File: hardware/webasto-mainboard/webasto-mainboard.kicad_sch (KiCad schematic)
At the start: 11 parts

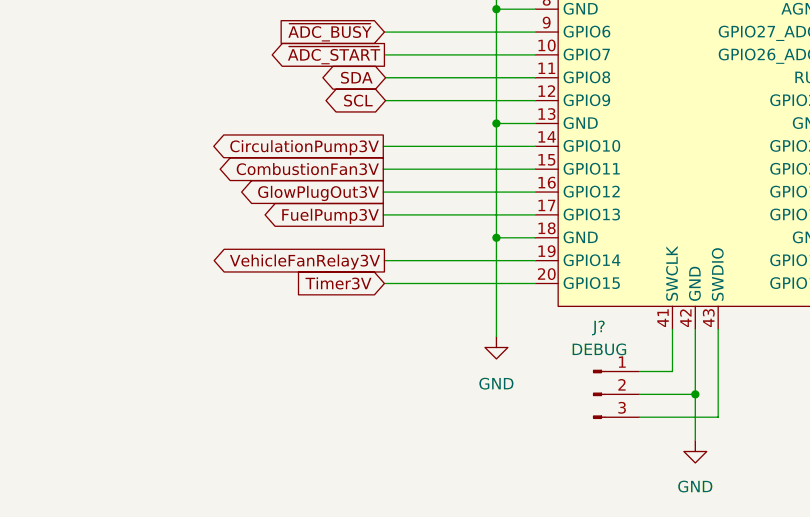
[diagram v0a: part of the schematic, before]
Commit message: Update schematics.  Had a better idea.
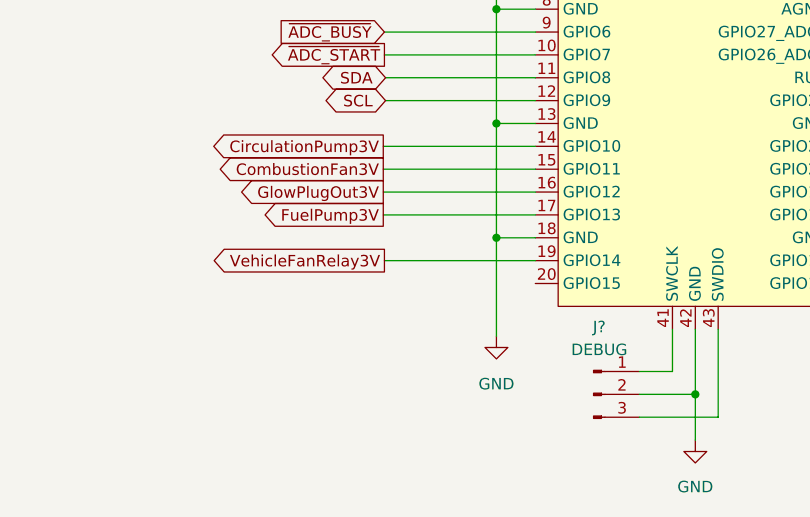
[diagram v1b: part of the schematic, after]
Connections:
- net Timer3V: no longer names the net of U?.20 (GPIO15)
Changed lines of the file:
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@@
-    (stroke (width 0) (type default) (color 0 0 0 0))
-  )
-  (wire (pts (xy 109.855 144.653) (xy 126.619 144.653))
     (stroke (width 0) (type default) (color 0 0 0 0))
   )
@@
     (effects (font (size 1.27 1.27)) (justify right))
     (property "Intersheet References" "${INTERSHEET_REFS}" (id 0) (at 97.4633 98.8536 0)
-      (effects (font (size 1.27 1.27)) (justify right) hide)
-    )
-  )
-  (global_label "Timer3V" (shape input) (at 109.855 144.653 180) (fields_autoplaced)
-    (effects (font (size 1.27 1.27)) (justify right))
-    (property "Intersheet References" "${INTERSHEET_REFS}" (id 0) (at 100.0033 144.5736 0)
       (effects (font (size 1.27 1.27)) (justify right) hide)
     )
@@
       (reference "#PWR?") (unit 1) (value "+3V3") (footprint "")
     )
-    (path "/4eba7f3e-81ac-47cd-894e-cb117f012064/47587680-3503-46f7-a060-696a9c2f2074"
-      (reference "#PWR?") (unit 1) (value "+12V") (footprint "")
-    )
     (path "/5110a3f4-f5cf-4cd3-83b3-796c134e4e4f"
       (reference "#PWR?") (unit 1) (value "GND") (footprint "")
@@
       (reference "#PWR?") (unit 1) (value "+12V") (footprint "")
     )
-    (path "/4eba7f3e-81ac-47cd-894e-cb117f012064/d24087ff-492d-4dd2-be32-3f2b4a040185"
-      (reference "#PWR?") (unit 1) (value "+3V3") (footprint "")
-    )
     (path "/a592a926-6607-470c-8c00-8883e576bafe/d398396e-9d5c-4d0b-9432-67c25da39db5"
       (reference "#PWR?") (unit 1) (value "GND") (footprint "")
@@
       (reference "Q?") (unit 1) (value "2N7002") (footprint "Package_TO_SOT_SMD:SOT-23")
     )
-    (path "/4eba7f3e-81ac-47cd-894e-cb117f012064/11a8a387-60ef-4daa-b1f2-6a2e648a2221"
-      (reference "Q?") (unit 1) (value "2N7002") (footprint "Package_TO_SOT_SMD:SOT-23")
-    )
     (path "/4eba7f3e-81ac-47cd-894e-cb117f012064/5e743317-dee2-44eb-9fd1-c8d94f723e4f"
       (reference "Q?") (unit 1) (value "2N7002") (footprint "Package_TO_SOT_SMD:SOT-23")
@@
       (reference "R?") (unit 1) (value "1k3") (footprint "")
     )
-    (path "/4eba7f3e-81ac-47cd-894e-cb117f012064/668d7fe4-24e1-42ef-aa39-fe426461395d"
-      (reference "R?") (unit 1) (value "1k") (footprint "")
-    )
     (path "/4eba7f3e-81ac-47cd-894e-cb117f012064/714ffd75-9f9b-4ae8-9bd1-266ab07df269"
       (reference "R?") (unit 1) (value "1k") (footprint "")
@@
       (reference "R?") (unit 1) (value "10k0 1%") (footprint "")
     )
-    (path "/4eba7f3e-81ac-47cd-894e-cb117f012064/cf147a28-695e-4344-b1e9-1fec0a5746d6"
-      (reference "R?") (unit 1) (value "1k") (footprint "")
-    )
     (path "/a592a926-6607-470c-8c00-8883e576bafe/d74794f6-4920-4511-9e00-c57fc0bf000c"

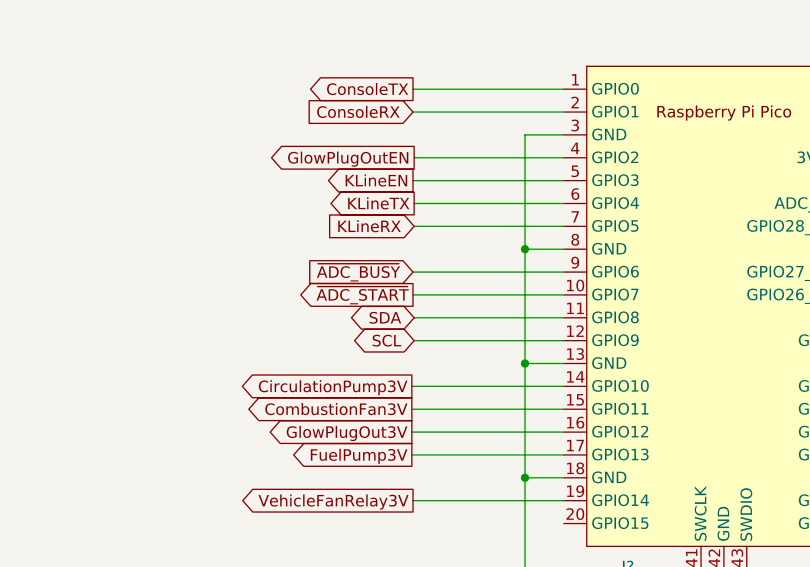
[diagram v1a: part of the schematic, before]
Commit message: Split out the sensor board for analog sensors
- Talks to the controller via I2C over a QWIIC chain.
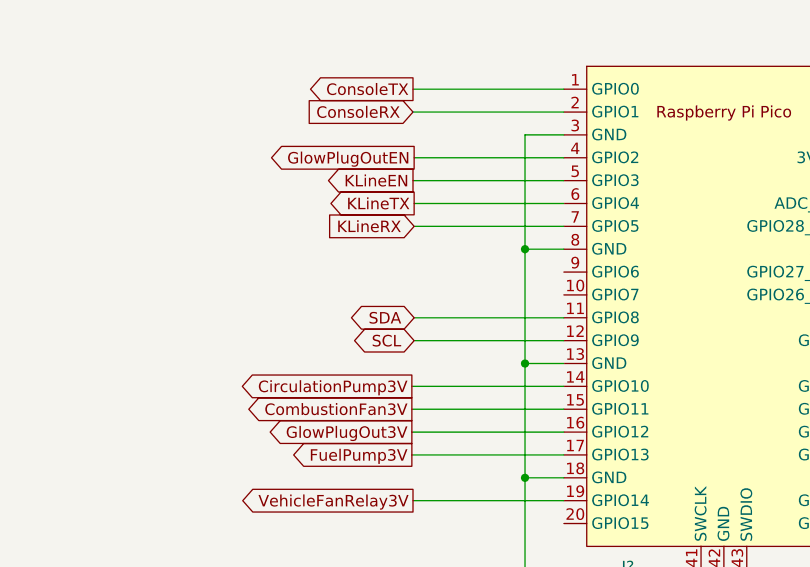
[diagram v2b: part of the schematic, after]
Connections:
- net ~{ADC_BUSY}: no longer names the net of U?.9 (GPIO6)
- net ~{ADC_START}: no longer names the net of U?.10 (GPIO7)
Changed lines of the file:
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@@
-    (stroke (width 0) (type default) (color 0 0 0 0))
-  )
-  (wire (pts (xy 109.855 119.253) (xy 126.619 119.253))
     (stroke (width 0) (type default) (color 0 0 0 0))
   )
@@
   )
   (wire (pts (xy 176.657 98.933) (xy 176.657 103.251))
-    (stroke (width 0) (type default) (color 0 0 0 0))
-  )
-  (wire (pts (xy 109.855 116.713) (xy 126.619 116.713))
     (stroke (width 0) (type default) (color 0 0 0 0))
   )
@@
     )
   )
-  (global_label "~{ADC_START}" (shape output) (at 109.855 119.253 180) (fields_autoplaced)
-    (effects (font (size 1.27 1.27)) (justify right))
-    (property "Intersheet References" "${INTERSHEET_REFS}" (id 0) (at 97.3424 119.1736 0)
-      (effects (font (size 1.27 1.27)) (justify right) hide)
-    )
-  )
   (global_label "GlowPlugOutEN" (shape output) (at 109.982 104.013 180) (fields_autoplaced)
     (effects (font (size 1.27 1.27)) (justify right))
@@
     (effects (font (size 1.27 1.27)) (justify right))
     (property "Intersheet References" "${INTERSHEET_REFS}" (id 0) (at 104.0613 124.2536 0)
-      (effects (font (size 1.27 1.27)) (justify right) hide)
-    )
-  )
-  (global_label "~{ADC_BUSY}" (shape input) (at 109.855 116.713 180) (fields_autoplaced)
-    (effects (font (size 1.27 1.27)) (justify right))
-    (property "Intersheet References" "${INTERSHEET_REFS}" (id 0) (at 97.9471 116.6336 0)
       (effects (font (size 1.27 1.27)) (justify right) hide)
     )
@@
     )
     (path "/7d073a75-c0a6-4467-8507-95514c8d14f0/022421ad-e4ba-4772-a24e-5b8b4cbfd678"
-      (reference "JX?") (unit 1) (value "6-pole connector") (footprint "")
+      (reference "JX1") (unit 1) (value "6-pole connector") (footprint "")
+    )
+    (path "/7d073a75-c0a6-4467-8507-95514c8d14f0/fdd36216-9c1a-49ce-9c2e-c88a03e20e50"
+      (reference "JX2") (unit 1) (value "2-pole connector") (footprint "")
+    )
+    (path "/7d073a75-c0a6-4467-8507-95514c8d14f0/de81a947-c9f1-467f-b9fd-935f16ddaae6"
+      (reference "JX3") (unit 1) (value "2-pole connector") (footprint "")
     )
     (path "/7d073a75-c0a6-4467-8507-95514c8d14f0/adcc54b0-88ab-4e99-abdb-30866c349bbc"
-      (reference "JX?") (unit 1) (value "2-pole connector") (footprint "")
+      (reference "JX4") (unit 1) (value "2-pole connector") (footprint "")
     )
     (path "/7d073a75-c0a6-4467-8507-95514c8d14f0/d81e4550-a768-4643-9327-8beb6b326cf3"
-      (reference "JX?") (unit 1) (value "2-pole connector") (footprint "")
-    )
-    (path "/7d073a75-c0a6-4467-8507-95514c8d14f0/de81a947-c9f1-467f-b9fd-935f16ddaae6"
-      (reference "JX?") (unit 1) (value "2-pole connector") (footprint "")
-    )
-    (path "/7d073a75-c0a6-4467-8507-95514c8d14f0/fdd36216-9c1a-49ce-9c2e-c88a03e20e50"
-      (reference "JX?") (unit 1) (value "2-pole connector") (footprint "")
+      (reference "JX5") (unit 1) (value "2-pole connector") (footprint "")
     )
     (path "/51487718-e94e-4b32-b7da-dfb4e19040ef/0d62e24c-7261-4a6c-a900-3ce0af2da1f5"

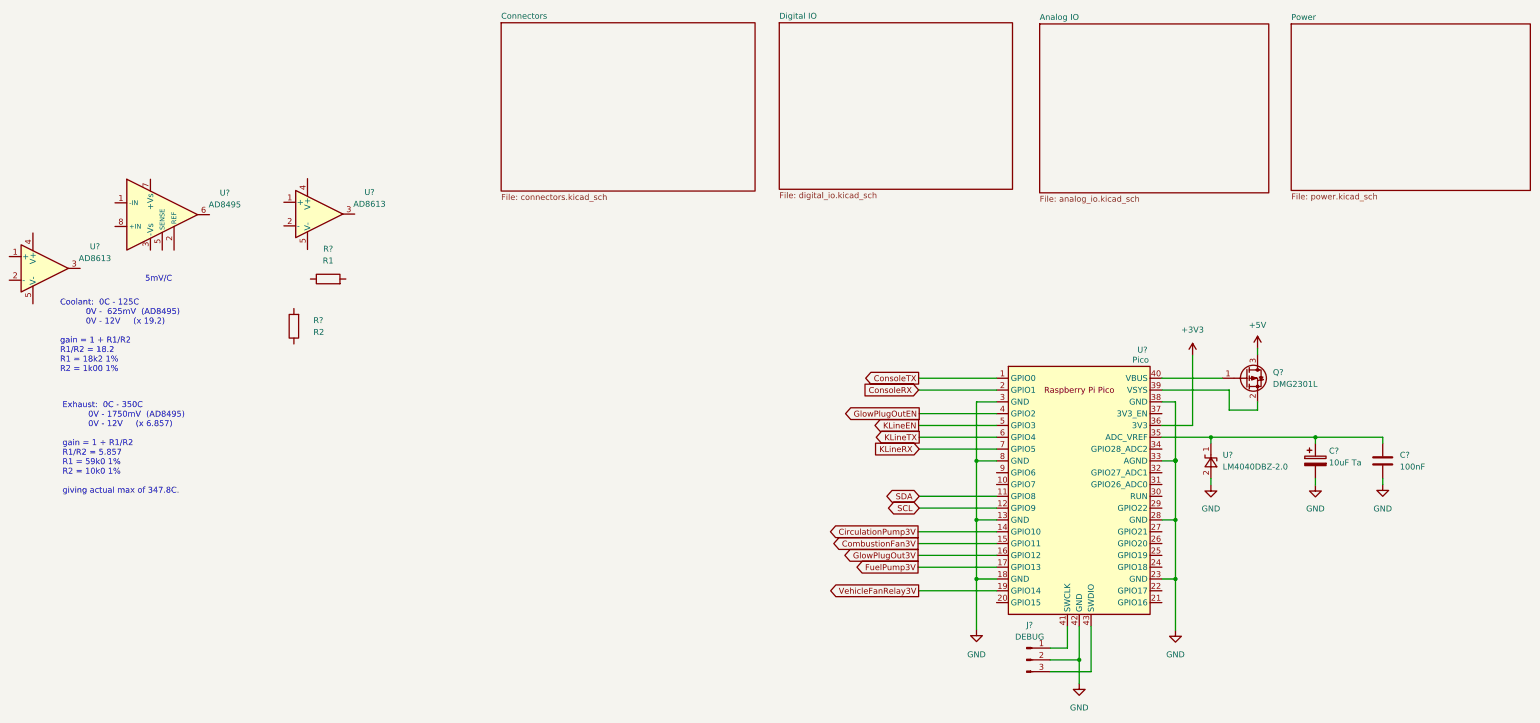
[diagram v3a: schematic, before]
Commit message: Added QWIIC Interface schematic, more cleanup
- redid all the MOSFET drives.  The fan one still concerns me a bit.
  is it supposed to DRIVE a relay, or BE a relay?  As long as it's a 12V
  relay, we should be good.
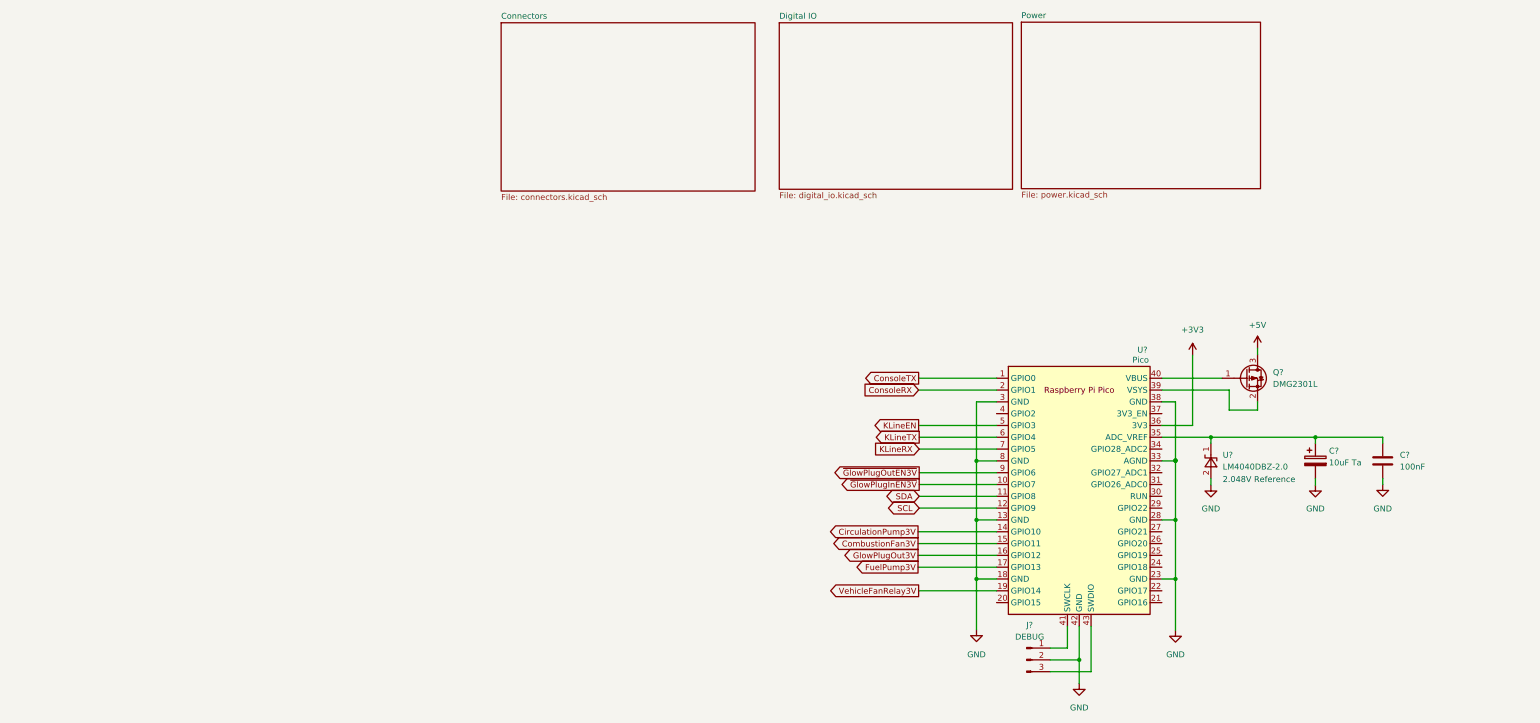
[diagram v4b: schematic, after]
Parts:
- removed R?: R2, symbol Device:R
- removed R?: R1, symbol Device:R
- removed U?: AD8495, Package_SO:MSOP-8_3x3mm_P0.65mm, symbol Sensor_Temperature:AD8495
- removed U? (x2): AD8613, symbol pspice:OPAMP
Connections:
- net ~{GlowPlugInEN3V}: now reaches U?.10 (GPIO7)
- net ~{GlowPlugOutEN3V}: now reaches U?.9 (GPIO6)
- net GlowPlugOutEN: no longer names the net of U?.4 (GPIO2)
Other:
- removed sheet Analog IO
- note added: "2.048V Reference"
- note removed: "5mV/C"
- note removed: "Coolant: 0C - 125C 0V - 625mV (AD8495) 0V - 12V (x 19.2) gain = 1 + R1/R2 R1/R2 = 18.2 R1 = 18k2 1% R2 = 1k00 1%"
- note removed: "Exhaust: 0C - 350C 0V - 1750mV (AD8495) 0V - 12V (x 6.857) gain = 1 + R1/R2 R1/R2 = 5.857 R1 = 59k0 1% R2 = 10k0 1% giving actual max of 347.8C."

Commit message: v1.0 layout complete
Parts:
- C1: renamed from C?; value 10uF Ta -> 10uF Ta 6V3; footprint (none) -> Capacitor_Tantalum_SMD:CP_EIA-3216-10_Kemet-I_Pad1.58x1.35mm_HandSolder
- C2: renamed from C?; footprint (none) -> Capacitor_SMD:C_0805_2012Metric_Pad1.18x1.45mm_HandSolder
- J1: renamed from J?; footprint (none) -> Connector_PinHeader_2.54mm:PinHeader_1x03_P2.54mm_Vertical
- gave numbers to parts that had none: 3
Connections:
- net ADC_VREF: now reaches C1.1, C2.1, U1.35 (ADC_VREF), U2.1 (K)
- net VSYS: now reaches Q1.2 (S), U1.39 (VSYS)
- net StartRun3V: now reaches U1.4 (GPIO2)
- net VBUS: now reaches Q1.1 (G), U1.40 (VBUS)

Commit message: Added title block info
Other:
- title: (none) -> Webasto Thermo Top C Replacement Controller
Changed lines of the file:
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@@
 (kicad_sch (version 20211123) (generator eeschema)
   (paper "A4")
+  (title_block
+    (title "Webasto Thermo Top C Replacement Controller")
+    (date "2023-01-19")
+    (rev "v1.0")
+  )
   (junction (at 122.301 114.173) (diameter 0) (color 0 0 0 0)
   )

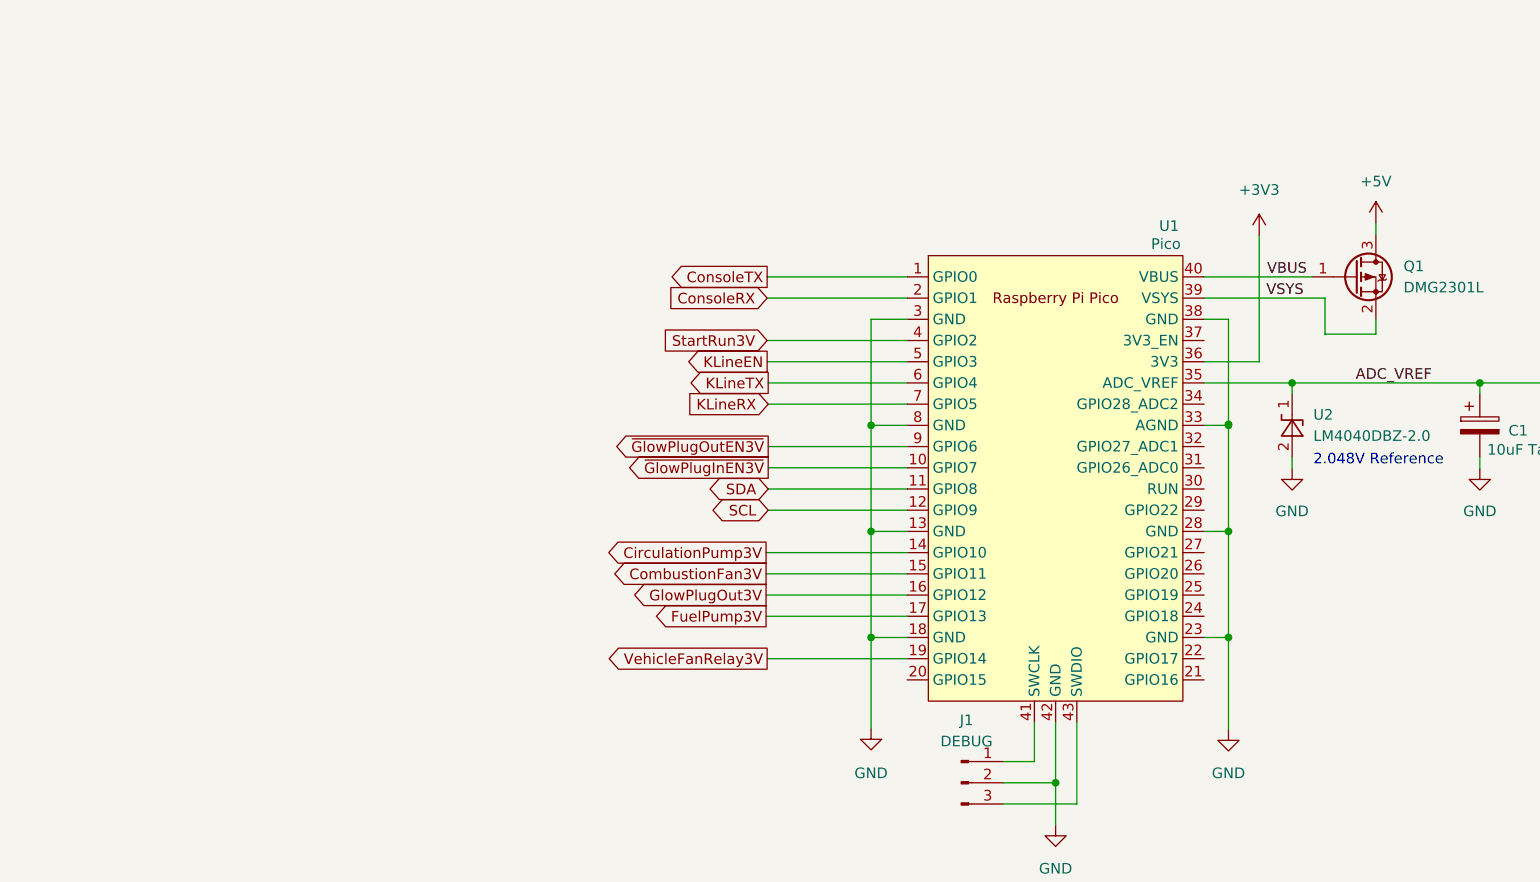
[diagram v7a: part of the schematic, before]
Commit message: Added logging, added debug serial to mainboard
- also added eeprom read support, and the digital GPIO over I2C
- route the ignition wire as a digital GPIO so we can use it as an input
  to the state machine.
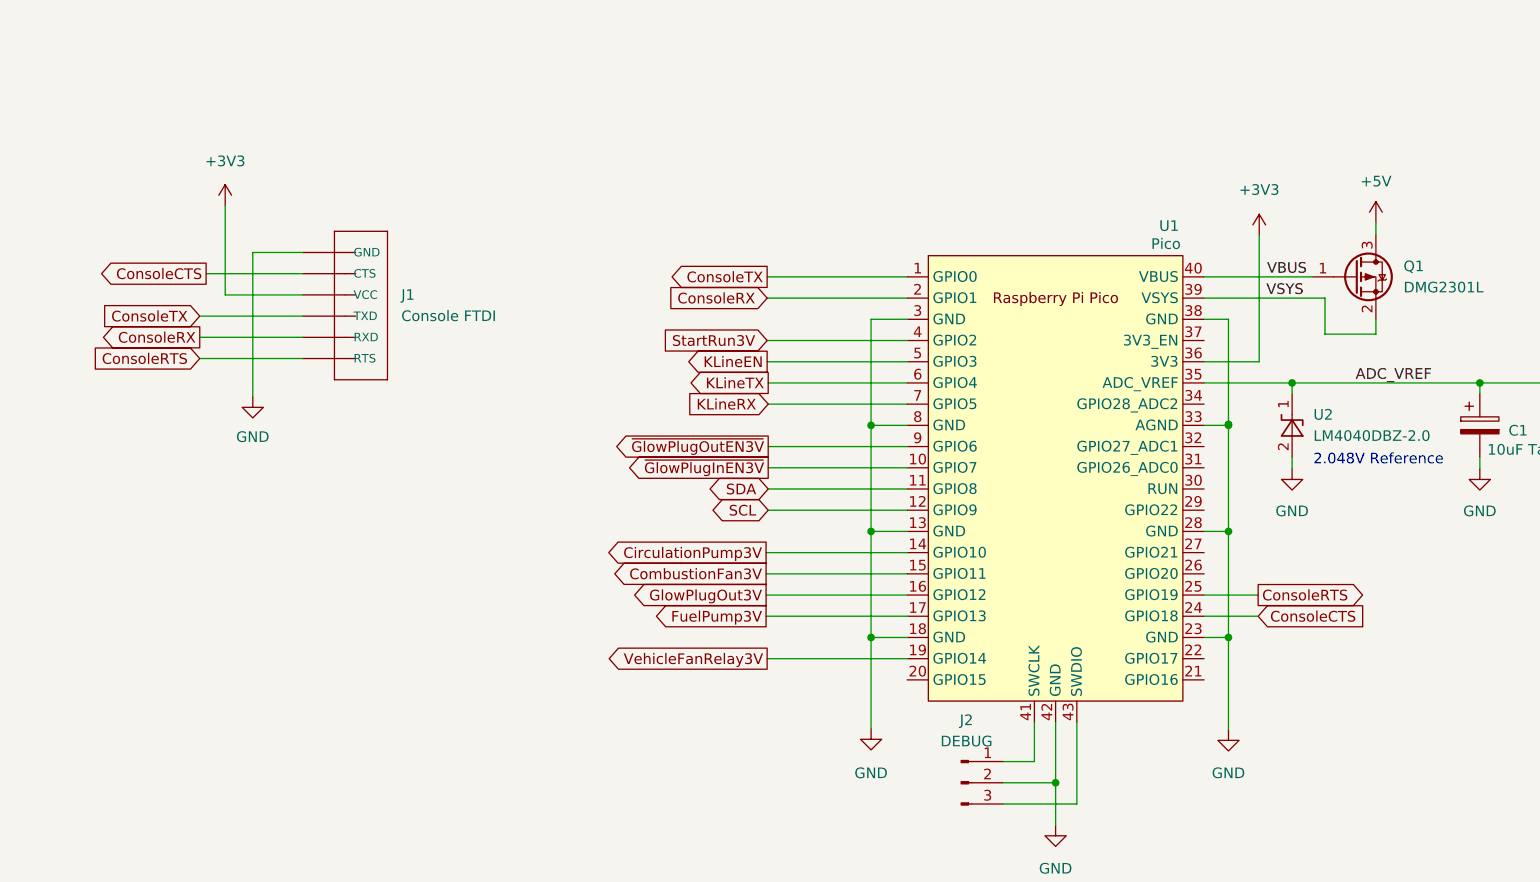
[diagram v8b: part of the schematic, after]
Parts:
- added J1: Console FTDI, FTDI_BASIC, symbol Beirdo:FTDI_BASICPTH
- renumbered J1 to J2
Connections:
- net +3V3: now also J1.3 (VCC)
- net ConsoleRX: now also J1.5 (RXD)
- net ConsoleTX: now also J1.4 (TXD)
- net GND: now also J1.1 (GND)
- net ConsoleCTS: now reaches U1.24 (GPIO18)
- net ConsoleCTS: now also J1.2 (CTS)
- net ConsoleRTS: now reaches U1.25 (GPIO19)
- net ConsoleRTS: now also J1.6 (RTS)
